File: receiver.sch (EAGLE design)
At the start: 27 parts

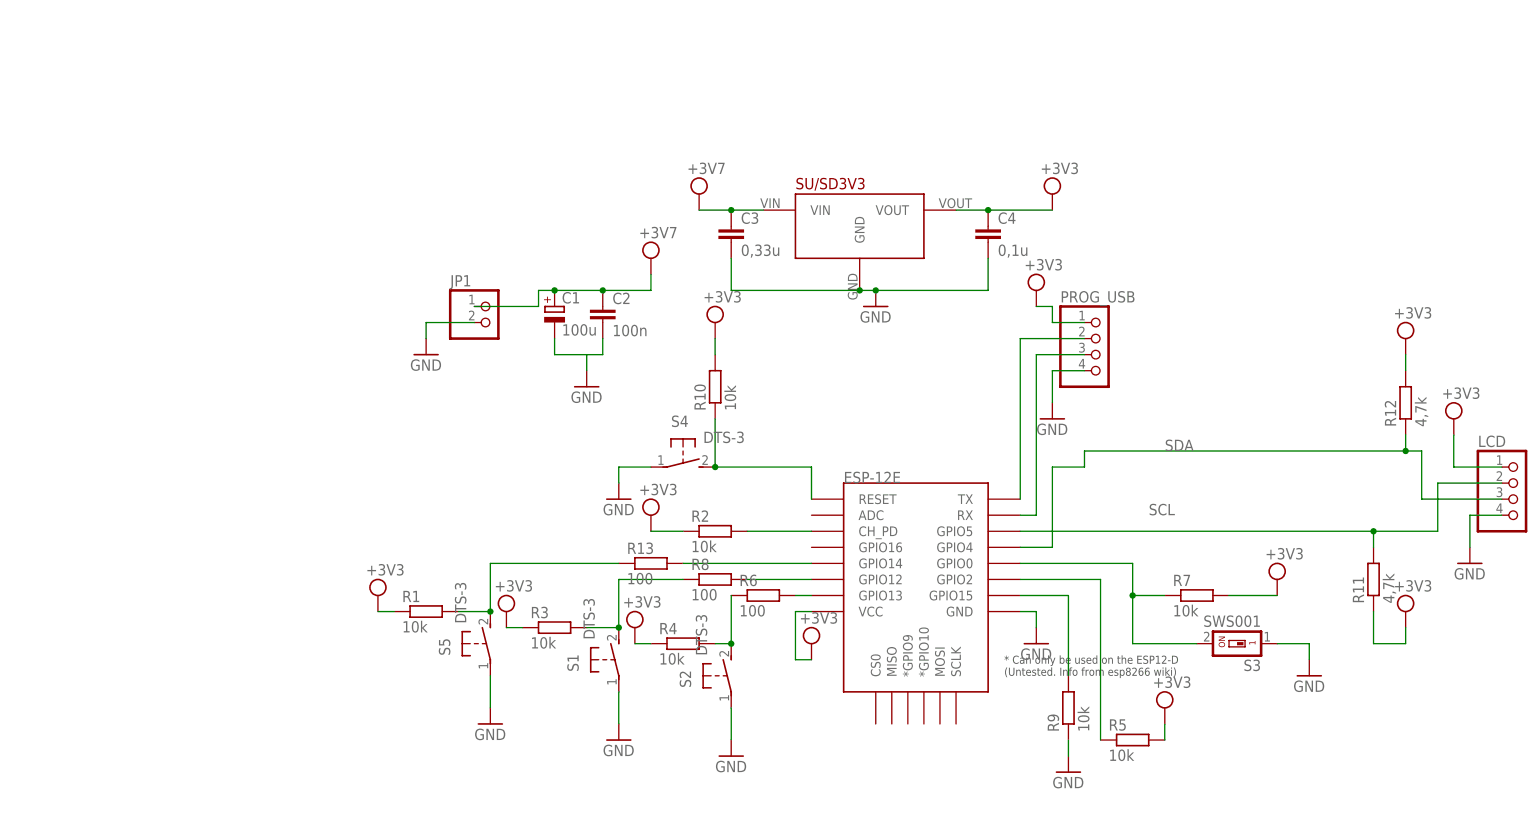
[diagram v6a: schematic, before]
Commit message: Added charger.
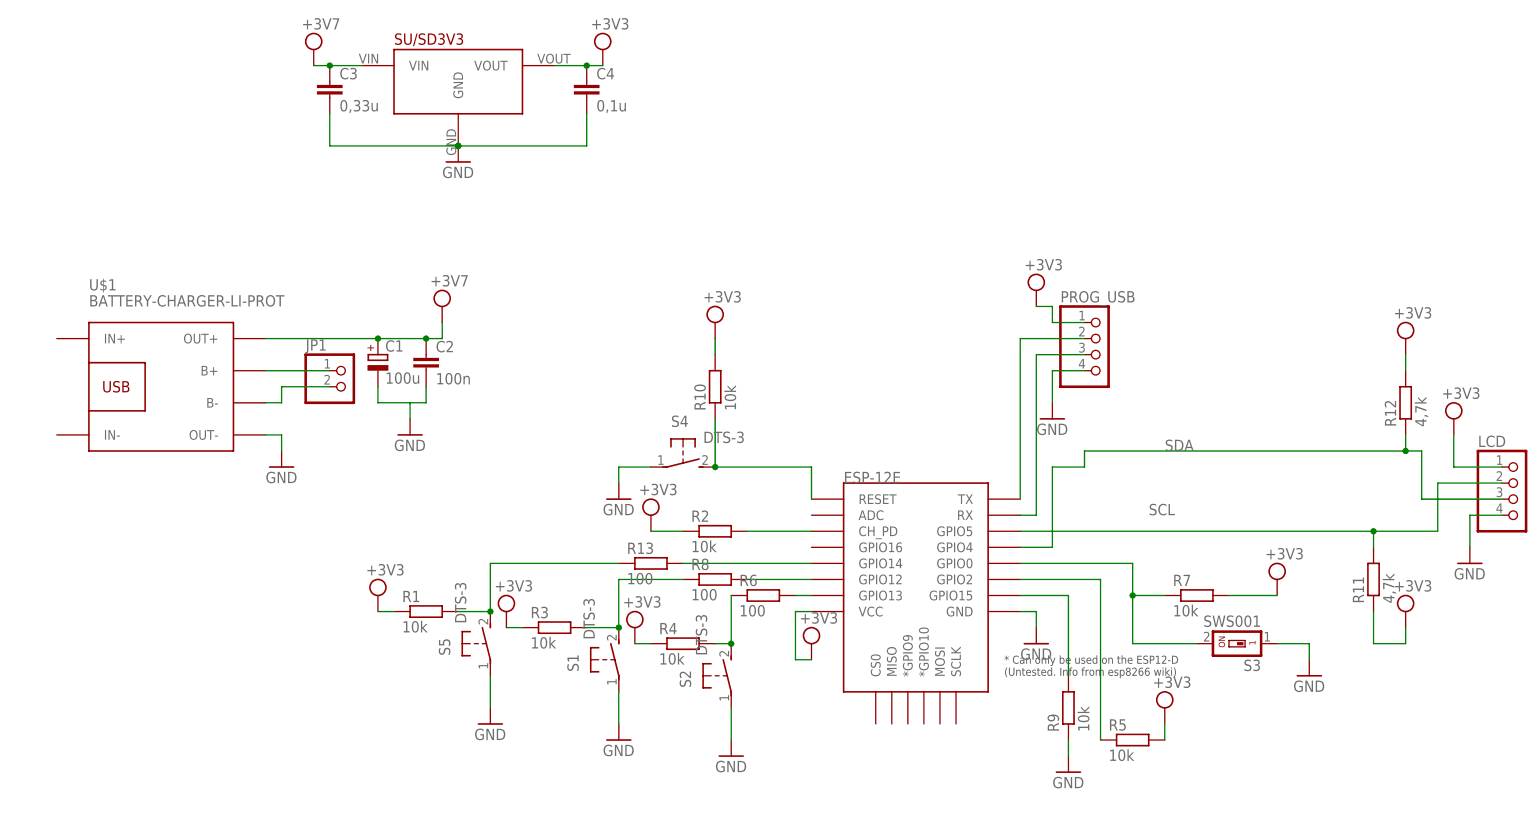
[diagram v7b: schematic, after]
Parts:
- added U$1: BATTERY-CHARGER-LI-PROT, diy-modules:BATTERY-CHARGER-LI-PROT
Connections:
- new net N$16: JP1.2, U$1.B-
- new net N$9: JP1.1, U$1.B+
- net GND: now also U$1.OUT-; no longer JP1.2
- net VCC: now also U$1.OUT+; no longer JP1.1
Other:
- moved on the sheet: C1, C2, C3, C4, JP1, SU/SD3V3
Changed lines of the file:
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@@
 <part name="GND7" library="supply1" library_urn="urn:adsk.eagle:library:371" deviceset="GND" device=""/>
 <part name="SUPPLY6" library="supply2" library_urn="urn:adsk.eagle:library:372" deviceset="VCC" device="" value="+3V3"/>
+<part name="U$1" library="diy-modules" deviceset="BATTERY-CHARGER-LI-PROT" device=""/>
 </parts>
 <sheets>
@@
 <instance part="R4" gate="G$1" x="20.32" y="50.8"/>
 <instance part="R5" gate="G$1" x="91.44" y="35.56"/>
-<instance part="C3" gate="G$1" x="27.94" y="116.84"/>
-<instance part="C4" gate="G$1" x="68.58" y="116.84"/>
-<instance part="GND5" gate="1" x="50.8" y="104.14"/>
-<instance part="JP1" gate="G$1" x="-10.16" y="101.6"/>
-<instance part="GND6" gate="1" x="-20.32" y="96.52"/>
-<instance part="SUPPLY9" gate="G$1" x="22.86" y="121.92"/>
+<instance part="C3" gate="G$1" x="-35.56" y="139.7"/>
+<instance part="C4" gate="G$1" x="5.08" y="139.7"/>
+<instance part="GND5" gate="1" x="-15.24" y="127"/>
+<instance part="JP1" gate="G$1" x="-33.02" y="91.44"/>
+<instance part="GND6" gate="1" x="-43.18" y="78.74"/>
+<instance part="SUPPLY9" gate="G$1" x="-38.1" y="144.78"/>
 <instance part="R6" gate="G$1" x="33.02" y="58.42"/>
-<instance part="C1" gate="G$1" x="0" y="104.14"/>
-<instance part="C2" gate="G$1" x="7.62" y="104.14"/>
-<instance part="SUPPLY3" gate="G$1" x="15.24" y="111.76"/>
-<instance part="GND8" gate="1" x="5.08" y="91.44"/>
+<instance part="C1" gate="G$1" x="-27.94" y="96.52"/>
+<instance part="C2" gate="G$1" x="-20.32" y="96.52"/>
+<instance part="SUPPLY3" gate="G$1" x="-17.78" y="104.14"/>
+<instance part="GND8" gate="1" x="-22.86" y="83.82"/>
 <instance part="R7" gate="G$1" x="101.6" y="58.42"/>
 <instance part="S3" gate="G$1" x="109.22" y="50.8" rot="R90"/>
@@
 <instance part="SUPPLY8" gate="G$1" x="25.4" y="101.6"/>
 <instance part="SUPPLY11" gate="G$1" x="15.24" y="71.12"/>
-<instance part="SUPPLY12" gate="G$1" x="78.74" y="121.92"/>
+<instance part="SUPPLY12" gate="G$1" x="7.62" y="144.78"/>
 <instance part="SUPPLY7" gate="G$1" x="142.24" y="86.36"/>
 <instance part="SUPPLY4" gate="G$1" x="-7.62" y="55.88"/>
@@
 <instance part="SUPPLY17" gate="G$1" x="134.62" y="99.06"/>
 <instance part="SUPPLY18" gate="G$1" x="134.62" y="55.88"/>
-<instance part="SU/SD3V3" gate="J_REG_5V" x="48.26" y="119.38"/>
+<instance part="SU/SD3V3" gate="J_REG_5V" x="-15.24" y="142.24"/>
 <instance part="S5" gate="G$1" x="-10.16" y="50.8"/>
 <instance part="R1" gate="G$1" x="-20.32" y="55.88"/>
@@
 <instance part="GND7" gate="1" x="-10.16" y="38.1"/>
 <instance part="SUPPLY6" gate="G$1" x="-27.94" y="58.42"/>
+<instance part="U$1" gate="G$1" x="-60.96" y="91.44"/>
 </instances>
 <busses>
@@
 <net name="VCC" class="0">
 <segment>
-<pinref part="JP1" gate="G$1" pin="1"/>
-<wire x1="-2.54" y1="106.68" x2="0" y2="106.68" width="0.1524" layer="91"/>
-<pinref part="C1" gate="G$1" pin="+"/>
-<pinref part="C2" gate="G$1" pin="1"/>
-<wire x1="0" y1="106.68" x2="7.62" y2="106.68" width="0.1524" layer="91"/>
-<junction x="0" y="106.68"/>
-<wire x1="7.62" y1="106.68" x2="15.24" y2="106.68" width="0.1524" layer="91"/>
-<junction x="7.62" y="106.68"/>
-<wire x1="15.24" y1="106.68" x2="15.24" y2="109.22" width="0.1524" layer="91"/>
-<pinref part="SUPPLY3" gate="G$1" pin="VCC"/>
-<wire x1="-12.7" y1="104.14" x2="-2.54" y2="104.14" width="0.1524" layer="91"/>
-<wire x1="-2.54" y1="104.14" x2="-2.54" y2="106.68" width="0.1524" layer="91"/>
-</segment>
-<segment>
 <pinref part="C3" gate="G$1" pin="1"/>
-<wire x1="27.94" y1="119.38" x2="22.86" y2="119.38" width="0.1524" layer="91"/>
+<wire x1="-35.56" y1="142.24" x2="-38.1" y2="142.24" width="0.1524" layer="91"/>
 <pinref part="SUPPLY9" gate="G$1" pin="VCC"/>
 <pinref part="SU/SD3V3" gate="J_REG_5V" pin="VIN"/>
-<wire x1="33.02" y1="119.38" x2="27.94" y2="119.38" width="0.1524" layer="91"/>
-<junction x="27.94" y="119.38"/>
+<wire x1="-30.48" y1="142.24" x2="-35.56" y2="142.24" width="0.1524" layer="91"/>
+<junction x="-35.56" y="142.24"/>
 </segment>
 <segment>
@@
 <segment>
 <pinref part="C4" gate="G$1" pin="1"/>
-<wire x1="68.58" y1="119.38" x2="78.74" y2="119.38" width="0.1524" layer="91"/>
+<wire x1="5.08" y1="142.24" x2="7.62" y2="142.24" width="0.1524" layer="91"/>
 <pinref part="SUPPLY12" gate="G$1" pin="VCC"/>
 <pinref part="SU/SD3V3" gate="J_REG_5V" pin="VOUT"/>
-<wire x1="63.5" y1="119.38" x2="68.58" y2="119.38" width="0.1524" layer="91"/>
-<junction x="68.58" y="119.38"/>
+<wire x1="0" y1="142.24" x2="5.08" y2="142.24" width="0.1524" layer="91"/>
+<junction x="5.08" y="142.24"/>
 </segment>
 <segment>
@@
 <wire x1="-27.94" y1="55.88" x2="-25.4" y2="55.88" width="0.1524" layer="91"/>
 </segment>
+<segment>
+<pinref part="C1" gate="G$1" pin="+"/>
+<pinref part="C2" gate="G$1" pin="1"/>
+<wire x1="-27.94" y1="99.06" x2="-20.32" y2="99.06" width="0.1524" layer="91"/>
+<pinref part="U$1" gate="G$1" pin="OUT+"/>
+<wire x1="-45.72" y1="99.06" x2="-27.94" y2="99.06" width="0.1524" layer="91"/>
+<junction x="-27.94" y="99.06"/>
+<wire x1="-20.32" y1="99.06" x2="-17.78" y2="99.06" width="0.1524" layer="91"/>
+<junction x="-20.32" y="99.06"/>
+<pinref part="SUPPLY3" gate="G$1" pin="VCC"/>
+<wire x1="-17.78" y1="99.06" x2="-17.78" y2="101.6" width="0.1524" layer="91"/>
+</segment>
 </net>
 <net name="GND" class="0">
@@
 </segment>
 <segment>
-<wire x1="50.8" y1="106.68" x2="48.26" y2="106.68" width="0.1524" layer="91"/>
-<wire x1="48.26" y1="106.68" x2="27.94" y2="106.68" width="0.1524" layer="91"/>
+<wire x1="-15.24" y1="129.54" x2="-35.56" y2="129.54" width="0.1524" layer="91"/>
 <pinref part="C3" gate="G$1" pin="2"/>
-<wire x1="27.94" y1="111.76" x2="27.94" y2="106.68" width="0.1524" layer="91"/>
+<wire x1="-35.56" y1="134.62" x2="-35.56" y2="129.54" width="0.1524" layer="91"/>
 <pinref part="GND5" gate="1" pin="GND"/>
 <pinref part="SU/SD3V3" gate="J_REG_5V" pin="GND"/>
-<junction x="48.26" y="106.68"/>
+<junction x="-15.24" y="129.54"/>
 <pinref part="C4" gate="G$1" pin="2"/>
-<wire x1="50.8" y1="106.68" x2="68.58" y2="106.68" width="0.1524" layer="91"/>
-<wire x1="68.58" y1="106.68" x2="68.58" y2="111.76" width="0.1524" layer="91"/>
-<junction x="50.8" y="106.68"/>
-</segment>
-<segment>
-<pinref part="JP1" gate="G$1" pin="2"/>
-<wire x1="-12.7" y1="101.6" x2="-20.32" y2="101.6" width="0.1524" layer="91"/>
-<wire x1="-20.32" y1="101.6" x2="-20.32" y2="99.06" width="0.1524" layer="91"/>
-<pinref part="GND6" gate="1" pin="GND"/>
+<wire x1="-15.24" y1="129.54" x2="5.08" y2="129.54" width="0.1524" layer="91"/>
+<wire x1="5.08" y1="129.54" x2="5.08" y2="134.62" width="0.1524" layer="91"/>
+<junction x="-15.24" y="129.54"/>
 </segment>
 <segment>
@@
 <segment>
 <pinref part="C1" gate="G$1" pin="-"/>
-<wire x1="0" y1="99.06" x2="0" y2="96.52" width="0.1524" layer="91"/>
+<wire x1="-27.94" y1="91.44" x2="-27.94" y2="88.9" width="0.1524" layer="91"/>
 <pinref part="C2" gate="G$1" pin="2"/>
-<wire x1="5.08" y1="96.52" x2="7.62" y2="96.52" width="0.1524" layer="91"/>
-<wire x1="7.62" y1="96.52" x2="7.62" y2="99.06" width="0.1524" layer="91"/>
-<wire x1="0" y1="96.52" x2="5.08" y2="96.52" width="0.1524" layer="91"/>
-<wire x1="5.08" y1="96.52" x2="5.08" y2="93.98" width="0.1524" layer="91"/>
+<wire x1="-22.86" y1="88.9" x2="-20.32" y2="88.9" width="0.1524" layer="91"/>
+<wire x1="-20.32" y1="88.9" x2="-20.32" y2="91.44" width="0.1524" layer="91"/>
+<wire x1="-27.94" y1="88.9" x2="-22.86" y2="88.9" width="0.1524" layer="91"/>
+<wire x1="-22.86" y1="88.9" x2="-22.86" y2="86.36" width="0.1524" layer="91"/>
 <pinref part="GND8" gate="1" pin="GND"/>
 </segment>
@@
 <pinref part="GND7" gate="1" pin="GND"/>
 <wire x1="-10.16" y1="45.72" x2="-10.16" y2="40.64" width="0.1524" layer="91"/>
+</segment>
+<segment>
+<pinref part="GND6" gate="1" pin="GND"/>
+<wire x1="-43.18" y1="81.28" x2="-43.18" y2="83.82" width="0.1524" layer="91"/>
+<pinref part="U$1" gate="G$1" pin="OUT-"/>
+<wire x1="-43.18" y1="83.82" x2="-45.72" y2="83.82" width="0.1524" layer="91"/>
 </segment>
 </net>
@@
 </segment>
 </net>
+<net name="N$9" class="0">
+<segment>
+<pinref part="JP1" gate="G$1" pin="1"/>
+<pinref part="U$1" gate="G$1" pin="B+"/>
+<wire x1="-35.56" y1="93.98" x2="-45.72" y2="93.98" width="0.1524" layer="91"/>
+</segment>
+</net>
+<net name="N$16" class="0">
+<segment>
+<pinref part="U$1" gate="G$1" pin="B-"/>
+<wire x1="-45.72" y1="88.9" x2="-43.18" y2="88.9" width="0.1524" layer="91"/>
+<wire x1="-43.18" y1="88.9" x2="-43.18" y2="91.44" width="0.1524" layer="91"/>
+<pinref part="JP1" gate="G$1" pin="2"/>
+<wire x1="-43.18" y1="91.44" x2="-35.56" y2="91.44" width="0.1524" layer="91"/>
+</segment>
+</net>

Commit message: Renamed labels.
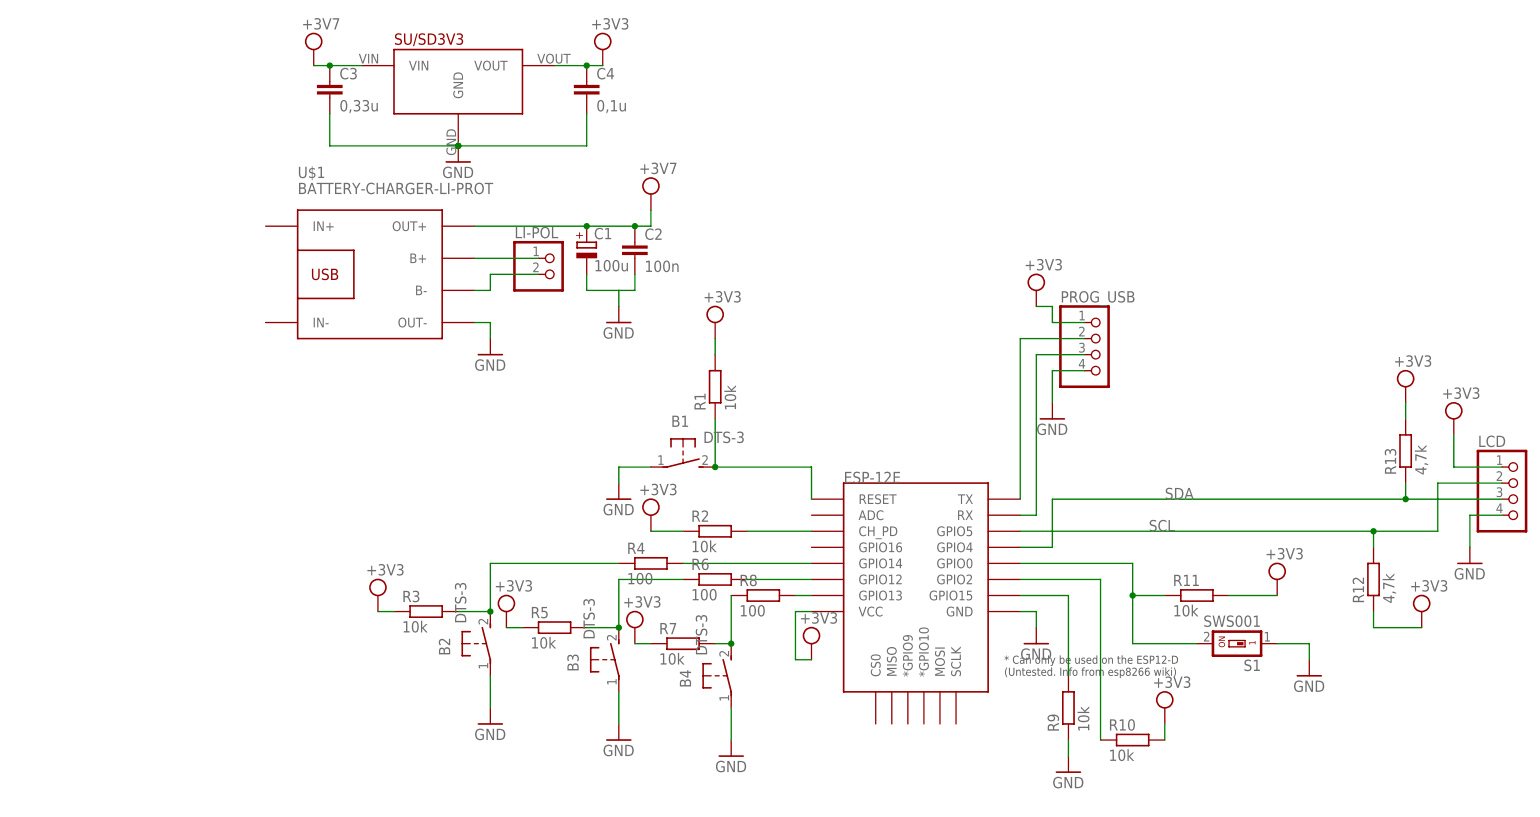
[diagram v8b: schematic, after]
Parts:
- removed JP1: (no value), pinhead:PINHD-1X2
- removed S3: SWS001, smd-special:SWS001
- added B3: DTS-3, switch-tact:DTS-3
- added LI-POL: (no value), pinhead:PINHD-1X2
- R11: value 4,7k -> 10k
- R13: value 100 -> 4,7k
- R4: value 10k -> 100
- S1: value DTS-3 -> SWS001; device switch-tact:DTS-3 -> smd-special:SWS001
- renumbered S2 to B4, S4 to B1, S5 to B2
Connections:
- net GND: now also B3.1; no longer S3.1
- net N$1: now also R1.1; no longer R10.1
- net N$10: now also R8.2; no longer R6.2
- net N$12: now also R4.2; no longer R13.2
- net N$13: now also R3.2, R4.1; no longer R1.2, R13.1
- net N$14: now also B3.2, R5.2, R6.1; no longer R3.2, R8.1, S1.2
- net N$16: now also LI-POL.2; no longer JP1.2
- net N$3: now also R11.1, S1.2; no longer R7.1, S3.2
- net N$4: now also R10.1; no longer R5.1
- net N$7: now also R6.2; no longer R8.2
- net N$8: now also R7.2, R8.1; no longer R4.2, R6.1
- net N$9: now also LI-POL.1; no longer JP1.1
- net SCL: now also R12.2; no longer R11.2
- net SDA: now also R13.1; no longer R12.1
- net VCC: now also R1.2, R11.2, R12.1, R13.2, R5.1, R7.1; no longer R1.1, R11.1, R12.2, R4.1, R5.2, R7.2
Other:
- moved on the sheet: C1, C2, R1, R10, R11, R12, R13, R3, R4, R5, R6, R7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
